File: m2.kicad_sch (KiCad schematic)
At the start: 19 parts, among them J5 Bus_M.2_1-2199230-6, U10 AP22615AWU-7, Y1 Oscillator_32.768kHz_OK2EL89C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

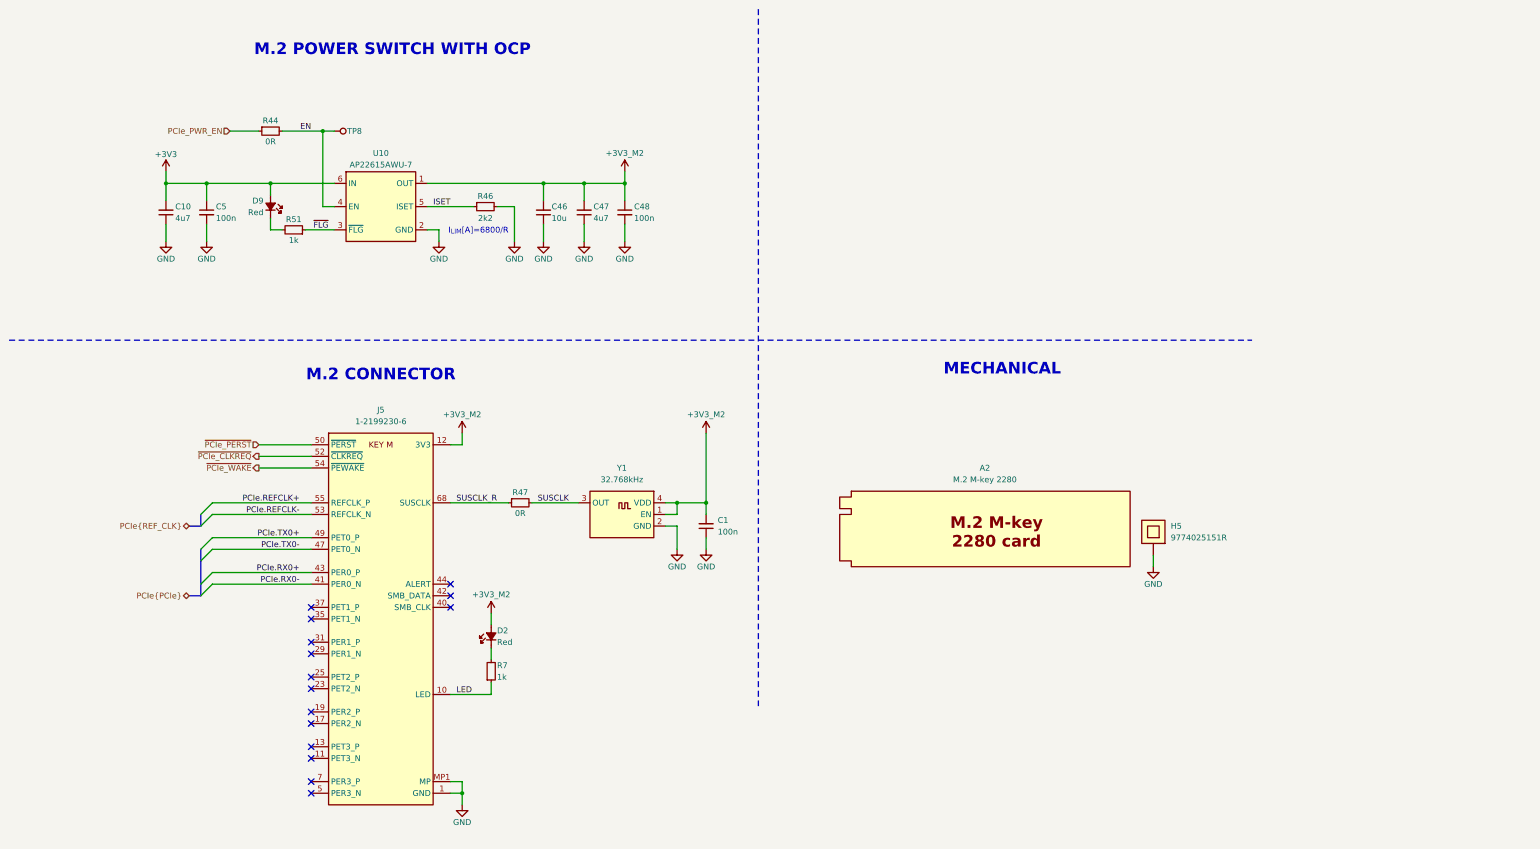
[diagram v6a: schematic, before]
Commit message: [#3] Layout USB power
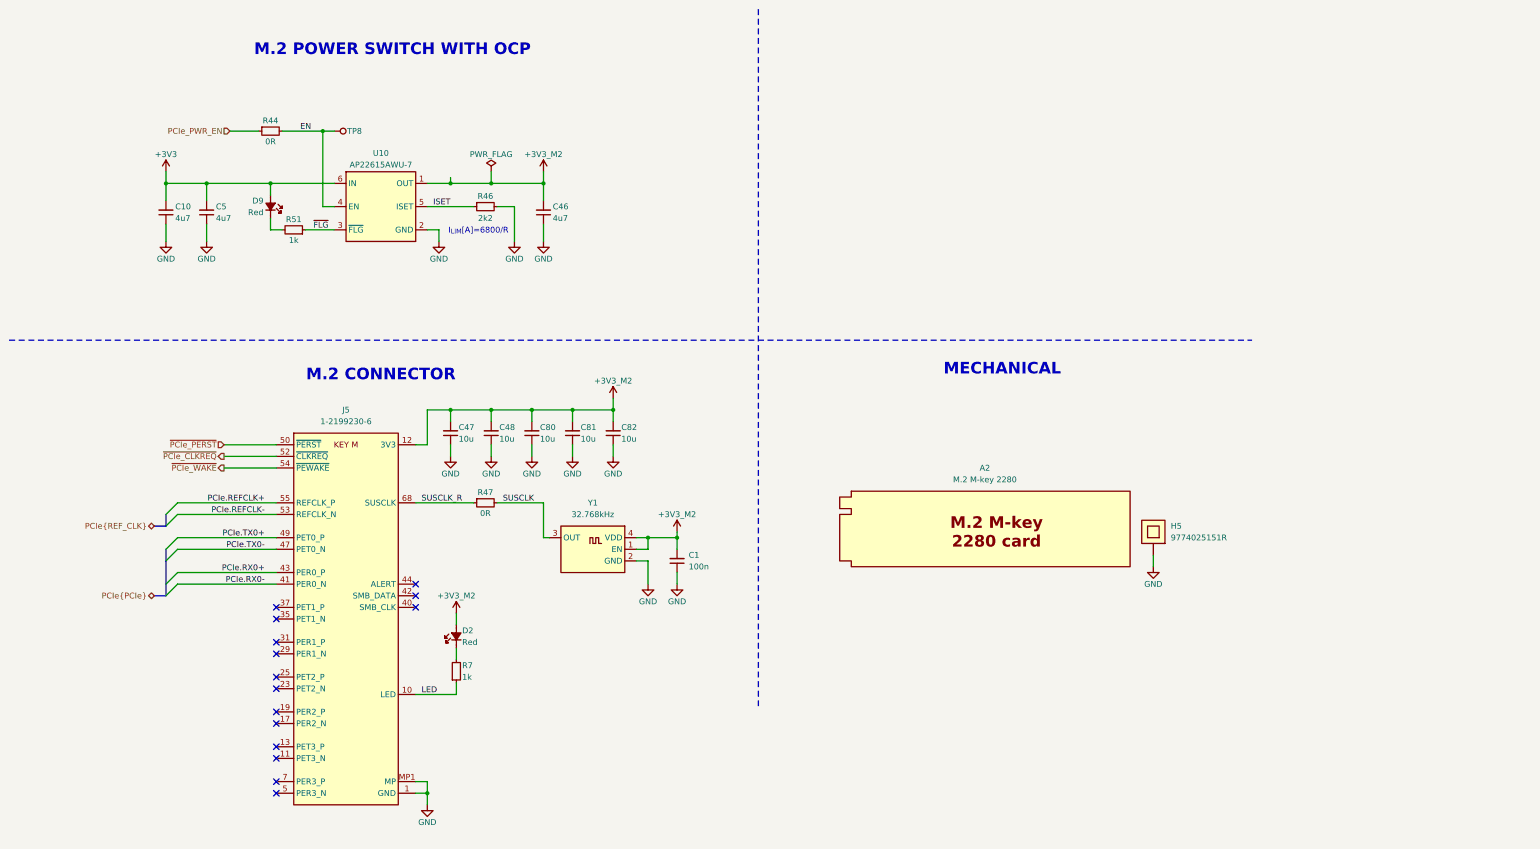
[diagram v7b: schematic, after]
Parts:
- removed C46: C-10u-0603, DW-footprints:C_0603_1608Metric, symbol DW-capacitors:C-10u-0603
- removed C47: C-4u7-0402, DW-footprints:C_0402_1005Metric, symbol DW-capacitors:C-4u7-0402
- removed C48, C5: C-100n-0402, DW-footprints:C_0402_1005Metric, symbol DW-capacitors:C-100n-0402
- added C46, C5: C-4u7-0402, DW-footprints:C_0402_1005Metric, symbol DW-capacitors:C-4u7-0402
- added C47, C48, C80, C81, C82: C-10u-0603, DW-footprints:C_0603_1608Metric, symbol DW-capacitors:C-10u-0603
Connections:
- net +3V3: now also C5.2
- net +3V3_M2: now also C46.2, C47.2, C48.2, C80.2, C81.2, C82.2
- net GND: now also C46.1, C47.1, C48.1, C5.1, C80.1, C81.1, C82.1
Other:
- moved on the sheet: C1, D2, J5, R47, R7, Y1

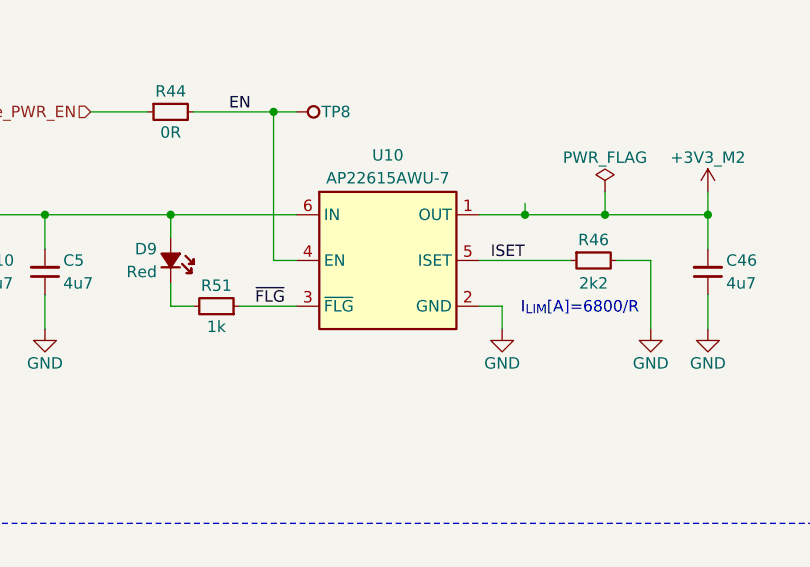
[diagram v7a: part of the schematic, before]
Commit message: [#3] Continue layout, minor schematic fixes, add power switch for CAN transceiver 5V rail
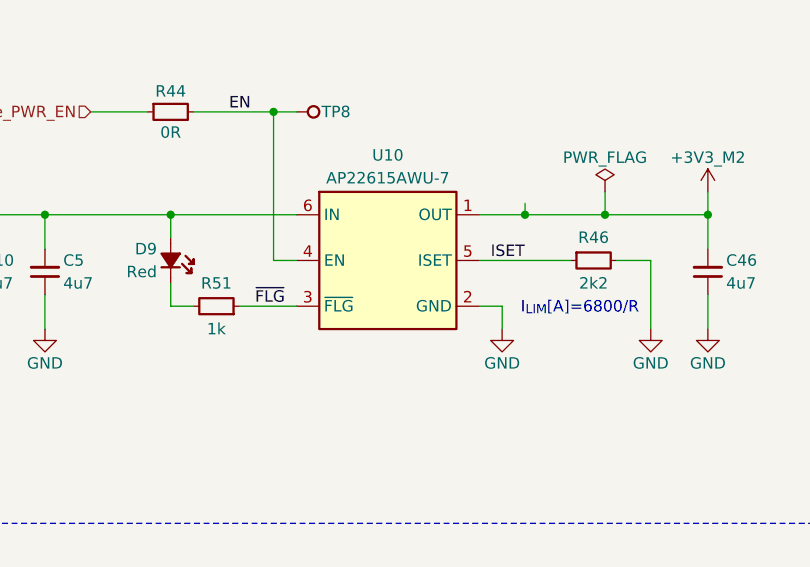
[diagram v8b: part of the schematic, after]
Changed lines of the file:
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@@
 		(dnp no)
 		(property "Reference" "R46"
-			(at 116.84 53.594 0)
+			(at 116.84 53.34 0)
 			(effects
 				(font
@@
 		(dnp no)
 		(property "Reference" "R51"
-			(at 74.93 58.674 0)
+			(at 74.93 58.42 0)
 			(effects
 				(font
@@
 		)
 		(property "Val" "1k"
-			(at 74.93 63.246 0)
-			(effects
-				(font
+			(at 74.93 63.5 0)
+			(effects
+				(font
